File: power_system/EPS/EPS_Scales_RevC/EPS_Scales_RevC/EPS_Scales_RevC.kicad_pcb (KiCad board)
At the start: 4 copper layers, 95.2 x 66 mm, 252 parts, among them J1 Input Power, J10 DF11-16DP-2DSA, J11 DN-T1-GE3_VIS, J12 DF11-16DP-2DSA, J15 DN-T1-GE3_VIS, J16 Conn_01x04, J18 Conn_01x04, J2 Conn_01x01_Socket, J3 Conn_01x01_Socket, J4 Conn_01x01_Socket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

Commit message: Revert "Luca branch v2"
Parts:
- removed C37: 10n, Capacitor_SMD:C_1210_3225Metric
- removed C38, C39: 22p, easyeda2kicad:C1206
- removed G*** (x3): LOGO, LOGO
- removed R39: 100k, Resistor_SMD:R_0603_1608Metric
- removed R40: 150k, Resistor_SMD:R_0603_1608Metric
- removed R41: 50k, Resistor_SMD:R_0603_1608Metric
- removed R42, R43, R44, R45, R46, R47: 10k, Resistor_SMD:R_0603_1608Metric
- removed TP17: TestPoint, TestPoint:TestPoint_Pad_1.0x1.0mm
- removed U9: LTC4300A-1, RevC Footprints:LTC4300A-1
- added C11: 22p, Capacitor_SMD:C_1210_3225Metric, F.Cu at (152.1, 64.8)
- added C50: 22p, Capacitor_SMD:C_1210_3225Metric, F.Cu at (125.0, 65.0)
- added JP6: SolderJumper_2_Open, Jumper:SolderJumper-2_P1.3mm_Open_RoundedPad1.0x1.5mm, F.Cu at (189.1, 70.5)
- added L1: 3.3u, RevC Footprints:XEL6030102MEC, F.Cu at (160.3, 41.4)
- added L2: 3.3u, RevC Footprints:XEL6030102MEC, F.Cu at (160.3, 50.0)
- added L6: 1u, RevC Footprints:XEL6030102MEC, F.Cu at (133.2, 41.8)
- added L7: 1u, RevC Footprints:XEL6030102MEC, F.Cu at (133.2, 50.4)
- added L8: 1u, RevC Footprints:XEL6030102MEC, F.Cu at (133.2, 59.0)
- C31: footprint easyeda2kicad:C1206 -> Capacitor_SMD:C_1210_3225Metric
- D1, D10, D12, D3, D7, D9: footprint RevC Footprints:SODFL2512X100N -> Diode_SMD:D_SOD-323
- L3: value 10u -> 3.3u; footprint easyeda2kicad:IND-SMD_L13.8-W12.6_MHCC12050 -> RevC Footprints:XEL6030102MEC
- L4: value 2.2u -> 1u; footprint RevC Footprints:XEL6030 -> RevC Footprints:XEL6030102MEC
- L5: value 3.3u -> 1u; footprint RevC Footprints:XEL6030 -> RevC Footprints:XEL6030102MEC
- R31: value 100k -> 1k
- R65, R9: value 3.0k -> 3k
- moved C3 99.4 mm to (98.5, 43.6), turned to -90 degrees
- moved J1 94.3 mm to (106.2, 38.3), turned to 0 degrees
- moved C2 92.5 mm to (102.8, 43.6), turned to -90 degrees
- moved C1 85.9 mm to (107.0, 43.6), turned to -90 degrees
- moved L5 70.4 mm to (187.7, 50.8)
- moved TP4 42.4 mm to (145.8, 25.8)
- moved TP2 41.9 mm to (148.0, 25.8)
- moved TP31 41.6 mm to (119.2, 26.2)
- moved TP29 41.6 mm to (121.3, 26.2)
- moved J2 40.4 mm to (90.0, 25.8)
- moved J3 38.5 mm to (202.5, 25.8)
- moved D12 38.3 mm to (174.7, 85.9)
- moved D10 38.2 mm to (181.2, 85.3)
- moved C62 37.7 mm to (187.3, 86.0)
- moved R96 37.7 mm to (184.2, 79.5)
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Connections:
- D1 pad 2: +5V_WD_J -> +5V_Perif
- D10 pad 2: +3.3V_OBC -> +5V_Perif
- J18 pad 1: +3.3V_OBC -> +5V_Perif
- J18 pad 2: +3.3V_OBC -> +5V_Perif
- J8 pad 1: +5V_WD_J -> +5V_Perif
- J8 pad 2: +5V_WD_J -> +5V_Perif
- L3 pad 2: Net-(U2-BIAS) -> Net-(L2-Pad1)
- L4 pad 1: Net-(U6-SW) -> Net-(L4-Pad1)
- L5 pad 1: Net-(U11-SW) -> Net-(U6-SW)
- L5 pad 2: Net-(U11-BIAS) -> Net-(L4-Pad1)
- R101 pad 2: +3.3V_OBC -> +5V_Perif
- U12 pad 2: SDA -> OBC SDA
- U12 pad 4: SDA -> OBC SDA
- U12 pad 5: SCL -> OBC SCL
- U3 pad 4: SDA -> OBC SDA
- U3 pad 5: SCL -> OBC SCL
- U8 pad 4: SDA -> OBC SDA
- U8 pad 5: SCL -> OBC SCL
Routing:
- net +3.3V_OBC: track 238.2 -> 97.2 mm
- net SDA: track 126.5 -> 0.00 mm, vias 6 -> 0
- net SCL: track 113.6 -> 0.00 mm, vias 4 -> 0
- net ~{OBC_Toggle_Perif}: track 59.0 -> 1.24 mm
- net OBC SDA: track 19.3 -> 67.7 mm, vias 1 -> 3
- net +5V_Perif: track 84.2 -> 130.6 mm, vias 5 -> 3
- net +20V_Jetson: track 56.0 -> 15.4 mm, vias 4 -> 2
- net OBC SCL: track 25.5 -> 63.8 mm, vias 1 -> 3
- net +V_Batt: track 143.8 -> 108.1 mm, vias 6 -> 3
- net +5V_WD_J: track 30.0 -> 0.00 mm
- net ~{OBC_Toggle_Jetson}: track 33.3 -> 16.6 mm, vias 0 -> 2
- net WDT_WDI_OBC: track 56.6 -> 41.7 mm
- net WDT_WDI_Jetson: track 51.3 -> 39.7 mm
- net ~{WD_TOGGLE_OBC}: track 57.7 -> 46.2 mm, vias 5 -> 4
- net GND: track 167.3 -> 157.7 mm, vias 93 -> 90
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- removed copper zone on In2.Cu, net +V_Batt
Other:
- board size 95.2 x 66 mm -> 120 x 73.2 mm
- board text removed: "Designed by Luca Lanzillotta"
- board text removed: "SCALES EPS Viking 1-A"
- board text removed: "this should work..."

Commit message: Update EPS_Scales_RevC.kicad_pcb
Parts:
- moved J3 8.17 mm to (194.7, 28.3)
- moved J4 7.68 mm to (194.8, 90.8)
- moved J1 5.06 mm to (107.1, 43.2)
- moved C1 5.06 mm to (107.9, 48.6)
- moved C2 5.06 mm to (103.7, 48.6)
- moved C3 5.06 mm to (99.4, 48.6)
- moved J2 2.50 mm to (89.9, 28.3)
- moved TP46 1.24 mm to (143.1, 37.2)
- moved TP1 1.16 mm to (147.8, 37.2)
- moved TP3 1.08 mm to (145.4, 37.1)
- moved TP2 1.02 mm to (149.0, 25.6)
- moved TP4 1.02 mm to (146.8, 25.6)
- moved J6 1.02 mm to (159.7, 31.6)
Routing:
- net +5V_Perif: track 130.6 -> 118.7 mm
- net WDT_WDI_Perif: track 50.9 -> 44.5 mm
- net +V_Batt: track 108.1 -> 101.9 mm
- net OBC SCL: track 63.8 -> 58.1 mm
- net Net-(J12-Pad13): track 4.78 -> 0.00 mm
- net Net-(J12-Pad11): track 4.71 -> 0.00 mm
- net ~{OBC_Toggle_OBC}: track 4.92 -> 0.37 mm
- net Net-(J12-Pad14): track 4.52 -> 0.00 mm
- net Net-(J12-Pad12): track 4.47 -> 0.00 mm
- net OBC SDA: track 67.7 -> 63.4 mm
- net WDT_WDI_OBC: track 41.7 -> 37.8 mm
- net WDT_WDI_Jetson: track 39.7 -> 37.1 mm
- net +3.3V_OBC: track 97.2 -> 95.1 mm
- net GND: track 157.7 -> 158.4 mm
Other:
- board size 120 x 73.2 mm -> 111.8 x 69.5 mm

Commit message: Layout Improvements
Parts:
- moved TP4 13.9 mm to (143.1, 39.0)
- moved TP29 13.8 mm to (125.2, 39.5)
- moved TP31 13.8 mm to (122.9, 39.5)
- moved TP2 13.4 mm to (147.8, 39.0)
- moved TP37 7.16 mm to (126.2, 42.5)
- moved TP38 5.10 mm to (127.5, 39.5)
- moved TP9 3.66 mm to (152.4, 39.0)
- moved TP8 3.53 mm to (154.7, 39.0)
- moved TP30 3.50 mm to (118.5, 39.5)
- moved TP28 3.50 mm to (120.7, 39.5)
- moved TP32 3.50 mm to (116.4, 39.5)
- moved TP46 3.06 mm to (140.7, 39.0)
- moved TP20 3.03 mm to (180.0, 40.4)
- moved C1 2.98 mm to (107.9, 51.6)
- moved C2 2.98 mm to (103.6, 51.6)
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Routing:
- net +3.3V_OBC: track 95.1 -> 180.4 mm, vias 14 -> 12
- net ~{OBC_Toggle_Perif}: track 1.24 -> 54.6 mm
- net OBC SCL: track 58.1 -> 84.8 mm
- net OBC SDA: track 63.4 -> 79.9 mm
- net +20V_Jetson: track 15.4 -> 30.2 mm, vias 2 -> 3
- net ~{OBC_Toggle_Jetson}: track 16.6 -> 28.5 mm
- net WDT_WDI_Jetson: track 37.1 -> 48.7 mm
- net +5V_Perif: track 118.7 -> 128.3 mm
- net Net-(J6-Pad14): track 0.11 -> 8.40 mm
- net Net-(J12-Pad12): track 0.00 -> 7.59 mm, vias 0 -> 1
- net Net-(J12-Pad14): track 0.00 -> 7.49 mm, vias 0 -> 1
- net Net-(J6-Pad12): track 0.11 -> 7.24 mm
- net Net-(J12-Pad13): track 0.00 -> 5.80 mm
- net Net-(J12-Pad11): track 0.00 -> 5.73 mm
- net Net-(J6-Pad13): track 0.00 -> 5.39 mm
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
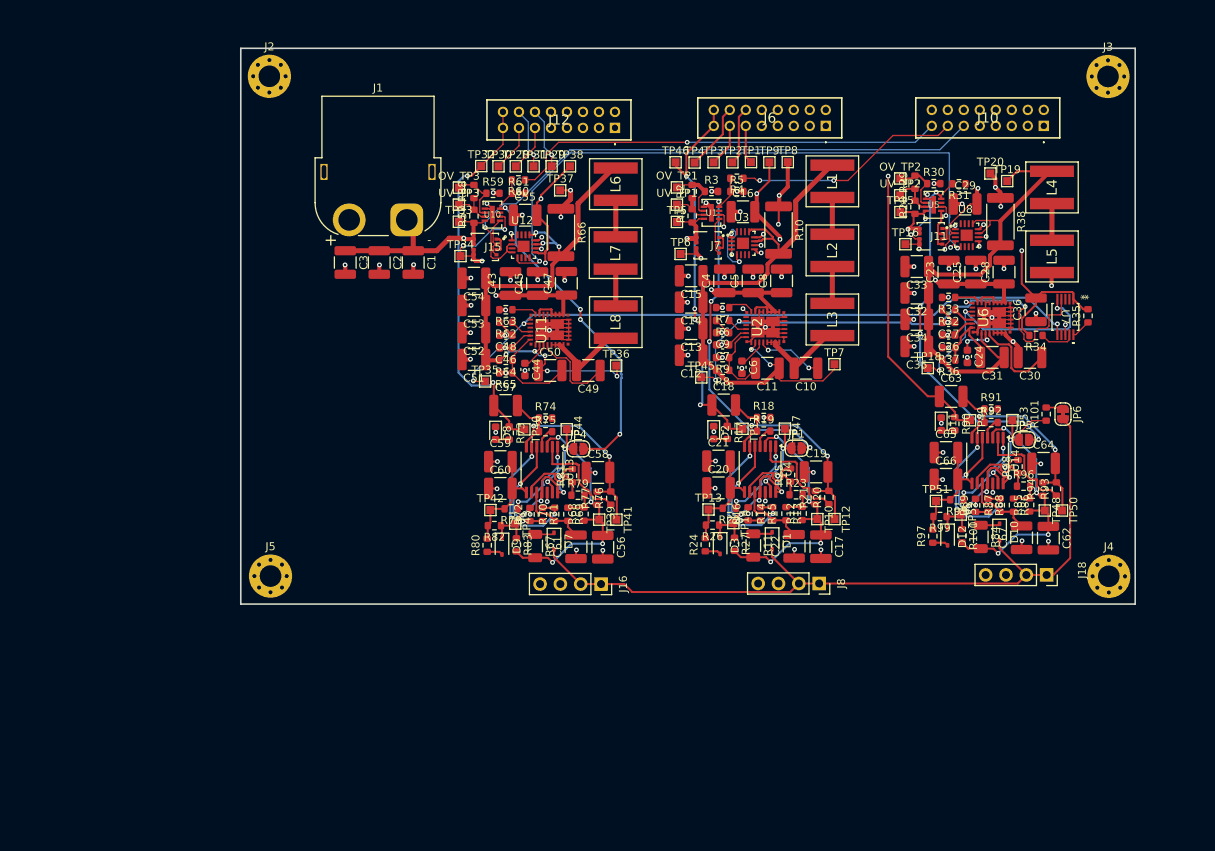
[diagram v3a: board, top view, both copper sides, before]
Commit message: Revisions to Schematic
Added request to add I2C buffer
Added request to modify block diagram to figure out WD con ops
Added pull up to OBC WD for proper SHDN use.
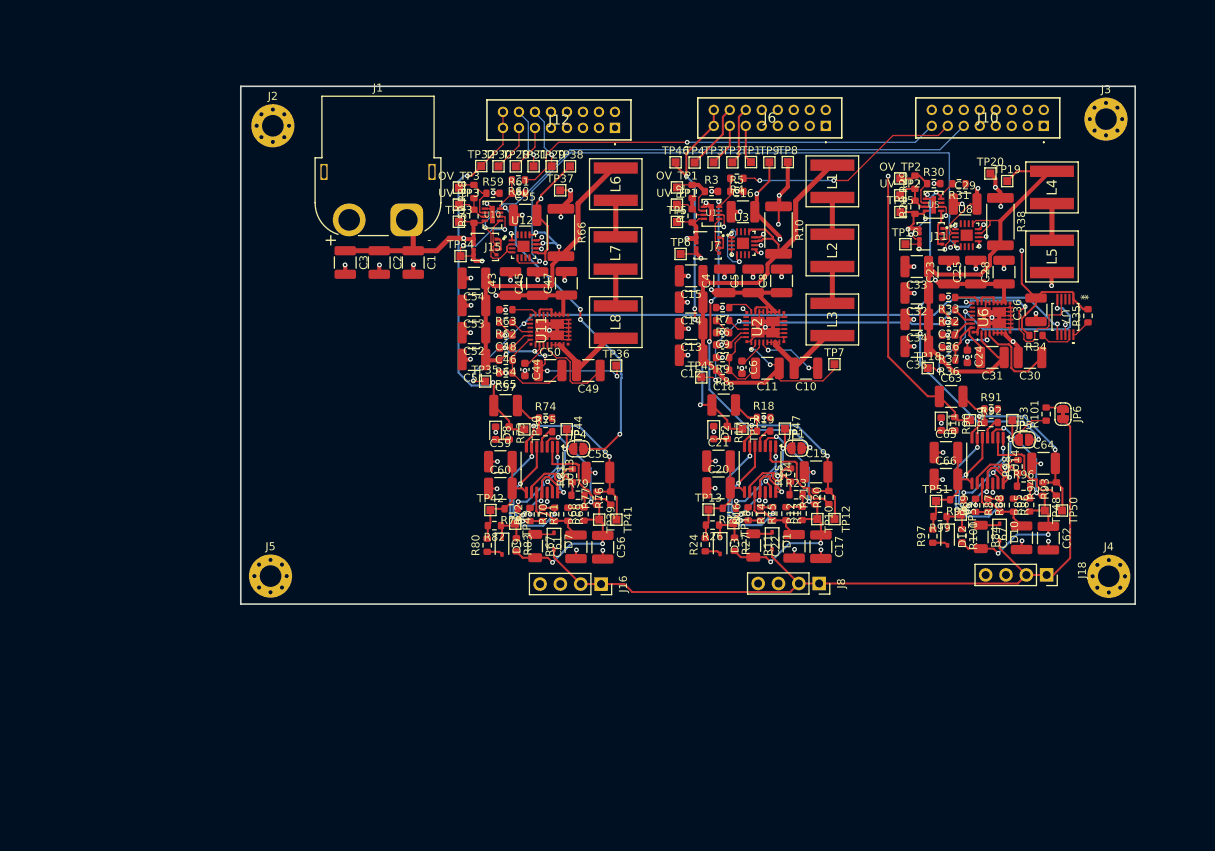
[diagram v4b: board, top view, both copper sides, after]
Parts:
- moved J2 6.20 mm to (90.3, 34.5)
- moved J3 5.33 mm to (194.5, 33.6)
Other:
- board size 111.8 x 69.5 mm -> 111.8 x 64.7 mm
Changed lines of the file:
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@@
 	(footprint "MountingHole:MountingHole_2.7mm_M2.5_Pad_Via"
 		(layer "F.Cu")
-		(at 89.9 28.275)
+		(at 90.331891 34.456891)
 		(descr "Mounting Hole 2.7mm")
 		(tags "mounting hole 2.7mm")
@@
 	(footprint "MountingHole:MountingHole_2.7mm_M2.5_Pad_Via"
 		(layer "F.Cu")
-		(at 194.725 28.3)
+		(at 194.475 33.625)
 		(descr "Mounting Hole 2.7mm")
 		(tags "mounting hole 2.7mm")
@@
 	)
 	(gr_rect
-		(start 86.325 24.775)
+		(start 86.325 29.525)
 		(end 198.125 94.25)
 		(stroke
@@
 		(polygon
 			(pts
-				(xy 198.15 25.075) (xy 198.125 58.975) (xy 197.925 94.025) (xy 86.325 93.975) (xy 86.6 25.15)
+				(xy 198.146576 29.717693) (xy 197.925 58.925) (xy 197.925 94.025) (xy 86.325 93.975) (xy 86.58145 29.792703)
 			)
 		)

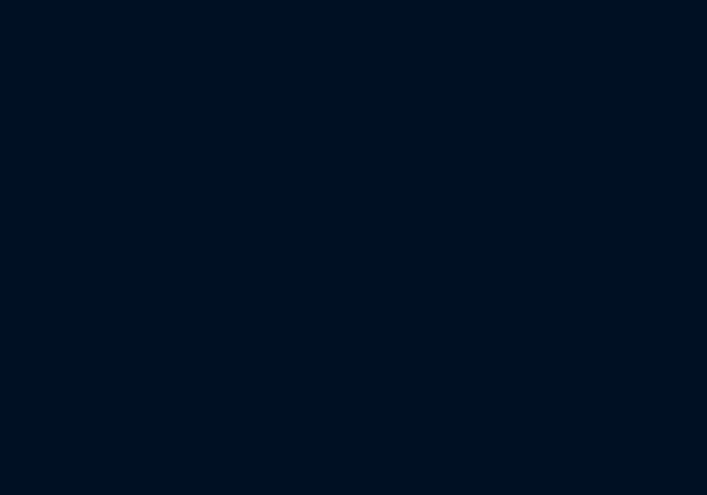
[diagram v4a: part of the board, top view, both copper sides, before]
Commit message: Schematic Revisions
Added I2c Buffer, not finished yet
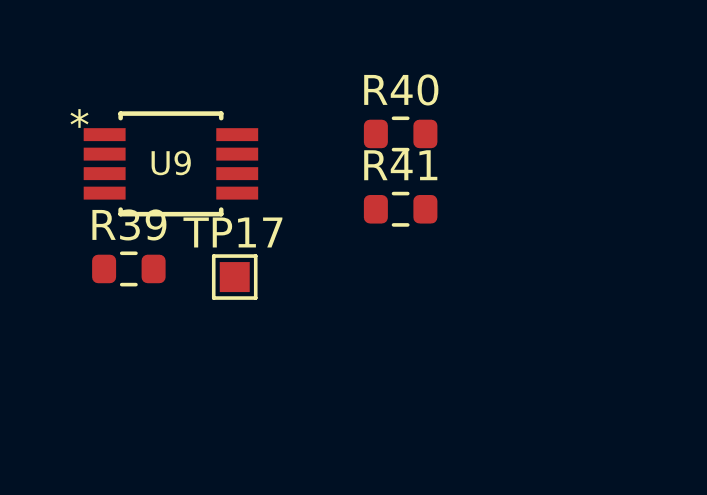
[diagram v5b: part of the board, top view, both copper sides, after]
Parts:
- added R39: 100k, Resistor_SMD:R_0603_1608Metric, F.Cu at (60.5, 34.3)
- added R40: 150k, Resistor_SMD:R_0603_1608Metric, F.Cu at (69.6, 29.8)
- added R41: 50k, Resistor_SMD:R_0603_1608Metric, F.Cu at (69.6, 32.3)
- added TP17: TestPoint, TestPoint:TestPoint_Pad_1.0x1.0mm, F.Cu at (64.1, 34.5)
- added U9: LTC4300A, REVC:LTC4300A, F.Cu at (61.9, 30.8)
- R31: value 1k -> 100k
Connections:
- D1 pad 2: +5V_Perif -> +5V_WD_J
- D10 pad 2: +5V_Perif -> +3.3V_OBC
- J18 pad 1: +5V_Perif -> +3.3V_OBC
- J18 pad 2: +5V_Perif -> +3.3V_OBC
- J8 pad 1: +5V_Perif -> +5V_WD_J
- J8 pad 2: +5V_Perif -> +5V_WD_J
- R101 pad 2: +5V_Perif -> +3.3V_OBC
- U12 pad 2: OBC SDA -> SDA
- U12 pad 4: OBC SDA -> SDA
- U12 pad 5: OBC SCL -> SCL
- U3 pad 4: OBC SDA -> SDA
- U3 pad 5: OBC SCL -> SCL
- U8 pad 4: OBC SDA -> SDA
- U8 pad 5: OBC SCL -> SCL
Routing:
- net SCL: track 0.00 -> 84.8 mm, vias 0 -> 3
- net OBC SCL: track 84.8 -> 0.00 mm, vias 3 -> 0
- net OBC SDA: track 79.9 -> 74.4 mm, vias 3 -> 1
- net SDA: track 0.00 -> 5.46 mm, vias 0 -> 2

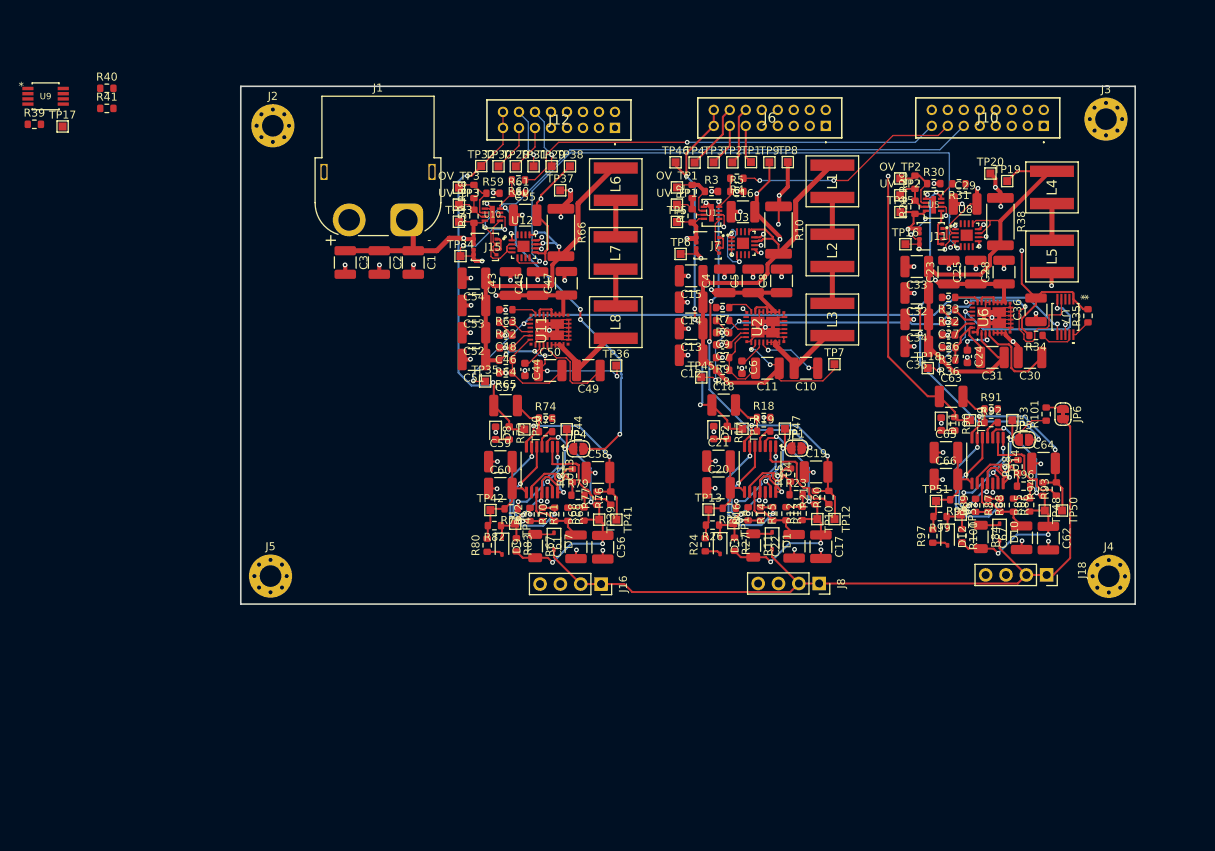
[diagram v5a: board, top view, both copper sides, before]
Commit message: Layout Complete
Added I2C buffer
Found replacement inductor for 10uH
Added footprints for new components
Last thing missing is changing the solder mask sizing on most footprints to remove the errors.
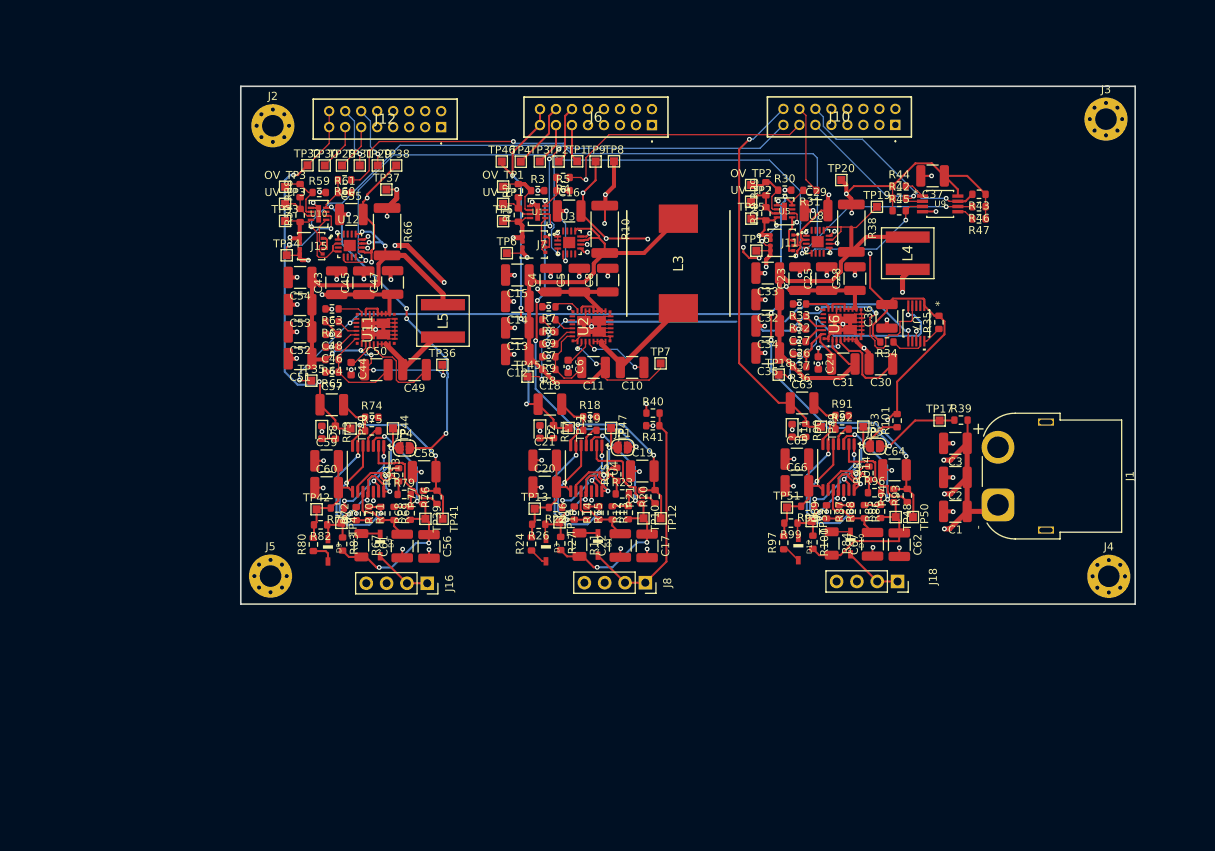
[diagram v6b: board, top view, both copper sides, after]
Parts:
- removed JP6: SolderJumper_2_Open, Jumper:SolderJumper-2_P1.3mm_Open_RoundedPad1.0x1.5mm
- removed L1, L2: 3.3u, RevC Footprints:XEL6030102MEC
- removed L6, L7, L8: 1u, RevC Footprints:XEL6030102MEC
- added C37: 0.01u, Capacitor_SMD:C_1210_3225Metric, F.Cu at (172.8, 40.7)
- added R42: 10k, Resistor_SMD:R_0603_1608Metric, F.Cu at (168.6, 43.5)
- added R43: 10k, Resistor_SMD:R_0603_1608Metric, F.Cu at (178.6, 43.0)
- added R44: 10k, Resistor_SMD:R_0603_1608Metric, F.Cu at (168.6, 42.0)
- added R45: 10k, Resistor_SMD:R_0603_1608Metric, F.Cu at (168.6, 45.1)
- added R46: 10k, Resistor_SMD:R_0603_1608Metric, F.Cu at (178.6, 44.6)
- added R47: 10k, Resistor_SMD:R_0603_1608Metric, F.Cu at (178.6, 46.1)
- D1, D10, D12, D3, D7, D9: footprint Diode_SMD:D_SOD-323 -> RevC Footprints:SODFL2512X100N
- L3: value 3.3u -> 10u; footprint RevC Footprints:XEL6030102MEC -> RevC Footprints:INDPM132129X640N
- L4: value 1u -> 2.2u; footprint RevC Footprints:XEL6030102MEC -> RevC Footprints:XEL6030
- L5: value 1u -> 3.3u; footprint RevC Footprints:XEL6030102MEC -> RevC Footprints:XEL6030
- U9: value LTC4300A -> LTC4300A-1; footprint REVC:LTC4300A -> RevC Footprints:LTC4300A-1
- moved R39 121.6 mm to (176.3, 71.2)
- moved TP17 115.6 mm to (173.7, 71.3)
- moved U9 112.6 mm to (173.8, 44.2)
- moved J1 82.0 mm to (181.0, 81.8), turned to -90 degrees
- moved C3 79.5 mm to (175.6, 74.2), turned to 180 degrees
- moved R40 79.4 mm to (137.8, 70.4)
- moved R41 78.9 mm to (137.8, 72.0), turned to 180 degrees
- moved C2 76.9 mm to (175.6, 78.4), turned to 180 degrees
- moved L5 76.6 mm to (111.6, 58.9)
- moved C1 74.6 mm to (175.6, 82.7), turned to 180 degrees
- moved D3 21.8 mm to (124.5, 87.5)
- moved D1 21.8 mm to (131.0, 86.8)
- moved D9 21.8 mm to (97.2, 87.5)
- moved D7 21.7 mm to (103.8, 86.9)
- moved R60 21.7 mm to (99.3, 41.2)
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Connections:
- L3 pad 2: Net-(L2-Pad1) -> Net-(U2-BIAS)
- L4 pad 1: Net-(L4-Pad1) -> Net-(U6-SW)
- L5 pad 1: Net-(U6-SW) -> Net-(U11-SW)
- L5 pad 2: Net-(L4-Pad1) -> Net-(U11-BIAS)
- U9 pad 1: unconnected-(U9-VCC2-Pad1) -> Net-(U9-ENABLE)
- U9 pad 2: unconnected-(U9-SCL_OUT-Pad2) -> OBC SDA
- U9 pad 3: unconnected-(U9-SCL_IN-Pad3) -> SCL
- U9 pad 4: unconnected-(U9-GND-Pad4) -> GND
- U9 pad 5: unconnected-(U9-READY-Pad5) -> Net-(U9-READY)
- U9 pad 6: unconnected-(U9-SDA_IN-Pad6) -> SDA
- U9 pad 7: unconnected-(U9-SDA_OUT-Pad7) -> OBC SCL
- U9 pad 8: unconnected-(U9-VCC-Pad8) -> +3.3V_OBC
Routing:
- net SDA: track 5.46 -> 126.5 mm, vias 2 -> 6
- net +V_Batt: track 101.0 -> 162.9 mm, vias 3 -> 6
- net OBC SDA: track 74.4 -> 19.3 mm
- net +3.3V_OBC: track 180.4 -> 235.1 mm, vias 12 -> 16
- net +5V_Perif: track 128.3 -> 84.6 mm, vias 3 -> 5
- net +5V_WD_J: track 0.00 -> 30.0 mm
- net SCL: track 84.8 -> 113.6 mm, vias 3 -> 4
- net +20V_Jetson: track 30.2 -> 56.1 mm, vias 3 -> 4
- net OBC SCL: track 0.00 -> 25.5 mm, vias 0 -> 1
- net WDT_WDI_OBC: track 36.5 -> 48.3 mm
- net ~{OBC_Toggle_OBC}: track 0.37 -> 11.4 mm
- net ~{WD_TOGGLE_OBC}: track 46.2 -> 56.1 mm
- net ~{OBC_Toggle_Jetson}: track 28.5 -> 33.3 mm, vias 2 -> 1
- net Net-(L7-Pad1): track 4.61 -> 0.00 mm
- net Net-(L2-Pad1): track 4.60 -> 0.00 mm
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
